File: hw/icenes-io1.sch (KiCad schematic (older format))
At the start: 12 parts

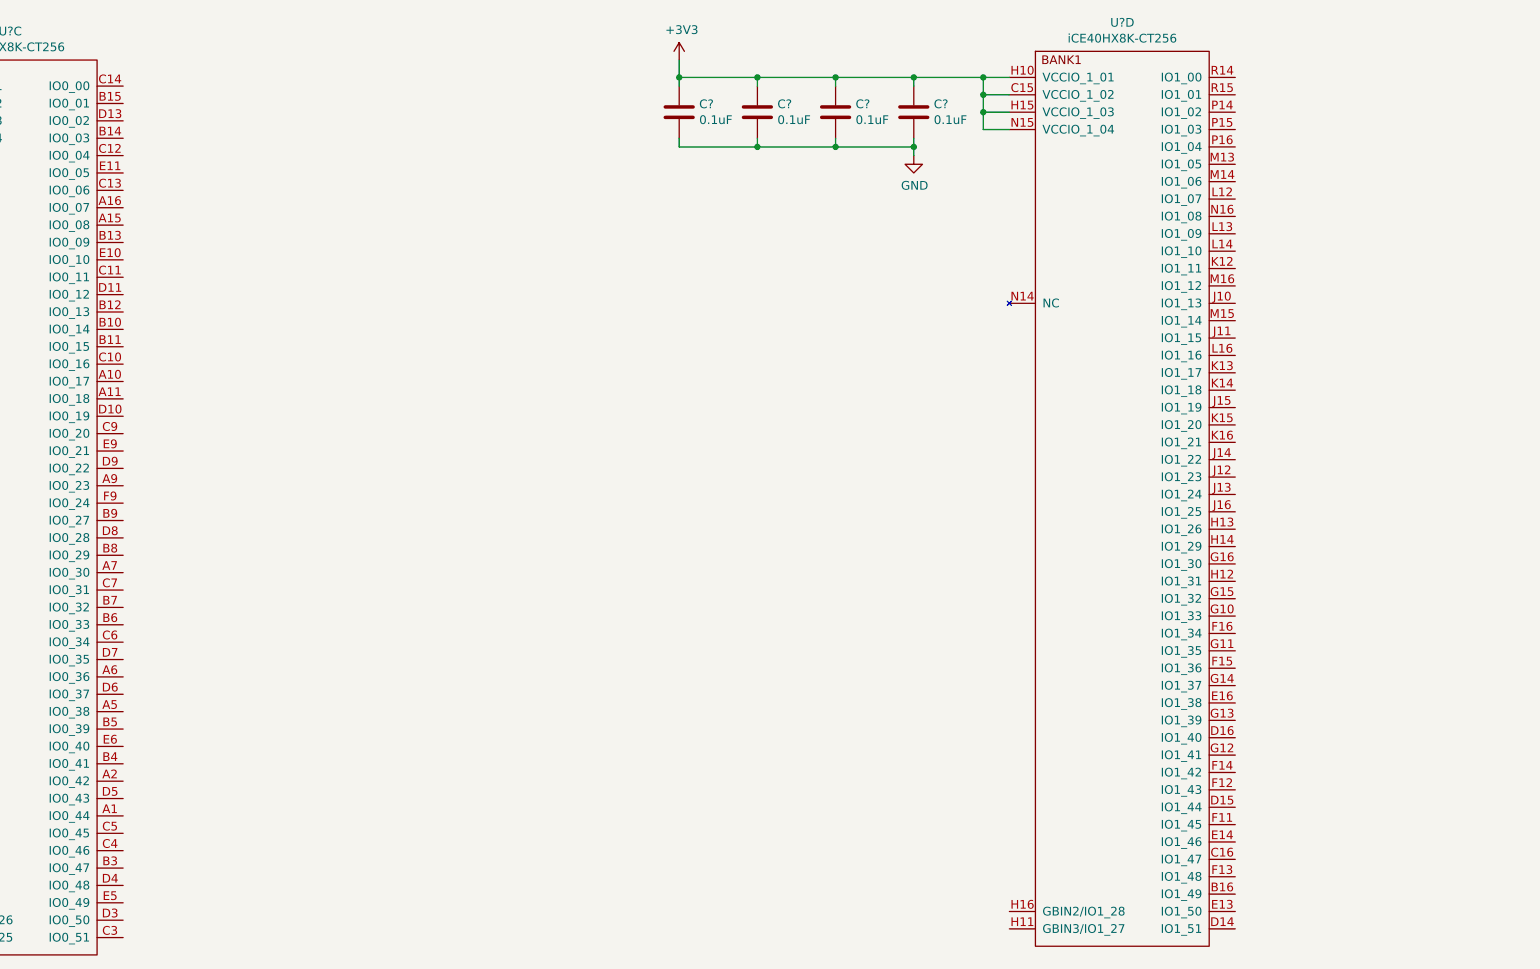
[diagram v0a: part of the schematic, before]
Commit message: Added voltage generators for 3.3V, 1.2V and 5V. Added more info and footprints to some components. Connected signals to the NES connector to banks 0 and 1.
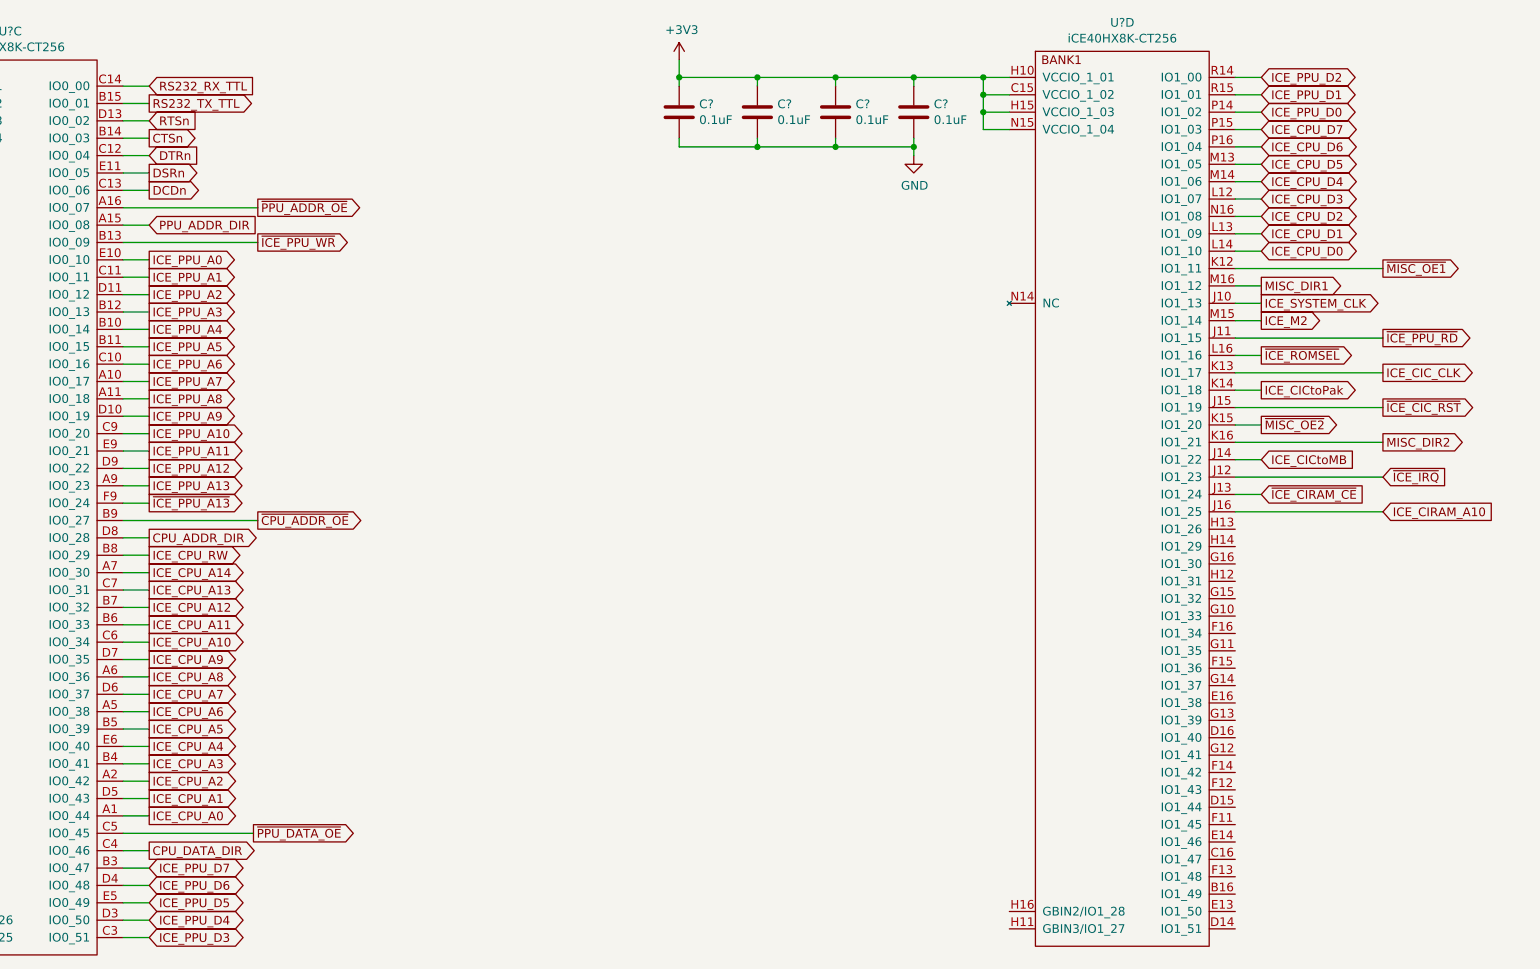
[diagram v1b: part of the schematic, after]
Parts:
- C? (x9): footprint (none) -> Capacitor_SMD:C_0603_1608Metric_Pad1.05x0.95mm_HandSolder; Manufacturer (none) -> Wurth; Part number (none) -> 885012206020
- C?: footprint (none) -> Capacitor_SMD:C_0603_1608Metric_Pad1.05x0.95mm_HandSolder; Manufacturer (none) -> Murata; Part number (none) -> GRM188R61A106KE69D
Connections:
- net ICE_CPU_A0: now reaches U?.A1 (IO0_44)
- net ICE_PPU_A7: now reaches U?.A10 (IO0_17)
- net ICE_PPU_A8: now reaches U?.A11 (IO0_18)
- net PPU_ADDR_DIR: now reaches U?.A15 (IO0_08)
- net ~PPU_ADDR_OE: now reaches U?.A16 (IO0_07)
- net ICE_CPU_A2: now reaches U?.A2 (IO0_42)
- net ICE_CPU_A6: now reaches U?.A5 (IO0_38)
- net ICE_CPU_A8: now reaches U?.A6 (IO0_36)
- net ICE_CPU_A14: now reaches U?.A7 (IO0_30)
- net ICE_PPU_A13: now reaches U?.A9 (IO0_23)
- net ICE_PPU_A4: now reaches U?.B10 (IO0_14)
- net ICE_PPU_A5: now reaches U?.B11 (IO0_15)
- net ICE_PPU_A3: now reaches U?.B12 (IO0_13)
- net ~ICE_PPU_WR: now reaches U?.B13 (IO0_09)
- net CTSn: now reaches U?.B14 (IO0_03)
- net RS232_TX_TTL: now reaches U?.B15 (IO0_01)
- net ICE_PPU_D7: now reaches U?.B3 (IO0_47)
- net ICE_CPU_A3: now reaches U?.B4 (IO0_41)
- net ICE_CPU_A5: now reaches U?.B5 (IO0_39)
- net ICE_CPU_A11: now reaches U?.B6 (IO0_33)
- net ICE_CPU_A12: now reaches U?.B7 (IO0_32)
- net ICE_CPU_RW: now reaches U?.B8 (IO0_29)
- net ~CPU_ADDR_OE: now reaches U?.B9 (IO0_27)
- net ICE_PPU_A6: now reaches U?.C10 (IO0_16)
- net ICE_PPU_A1: now reaches U?.C11 (IO0_11)
- net DTRn: now reaches U?.C12 (IO0_04)
- net DCDn: now reaches U?.C13 (IO0_06)
- net RS232_RX_TTL: now reaches U?.C14 (IO0_00)
- net ICE_PPU_D3: now reaches U?.C3 (IO0_51)
- net CPU_DATA_DIR: now reaches U?.C4 (IO0_46)
- net ~PPU_DATA_OE: now reaches U?.C5 (IO0_45)
- net ICE_CPU_A10: now reaches U?.C6 (IO0_34)
- net ICE_CPU_A13: now reaches U?.C7 (IO0_31)
- net ICE_PPU_A10: now reaches U?.C9 (IO0_20)
- net ICE_PPU_A9: now reaches U?.D10 (IO0_19)
- net ICE_PPU_A2: now reaches U?.D11 (IO0_12)
- net RTSn: now reaches U?.D13 (IO0_02)
- net ICE_PPU_D4: now reaches U?.D3 (IO0_50)
- net ICE_PPU_D6: now reaches U?.D4 (IO0_48)
- net ICE_CPU_A1: now reaches U?.D5 (IO0_43)
- net ICE_CPU_A7: now reaches U?.D6 (IO0_37)
- net ICE_CPU_A9: now reaches U?.D7 (IO0_35)
- net CPU_ADDR_DIR: now reaches U?.D8 (IO0_28)
- net ICE_PPU_A12: now reaches U?.D9 (IO0_22)
- net ICE_PPU_A0: now reaches U?.E10 (IO0_10)
- net DSRn: now reaches U?.E11 (IO0_05)
- net ICE_PPU_D5: now reaches U?.E5 (IO0_49)
- net ICE_CPU_A4: now reaches U?.E6 (IO0_40)
- net ICE_PPU_A11: now reaches U?.E9 (IO0_21)
- net ~ICE_PPU_A13: now reaches U?.F9 (IO0_24)
- net ICE_SYSTEM_CLK: now reaches U?.J10 (IO1_13)
- net ~ICE_PPU_RD: now reaches U?.J11 (IO1_15)
- net ~ICE_IRQ: now reaches U?.J12 (IO1_23)
- net ~ICE_CIRAM_CE: now reaches U?.J13 (IO1_24)
- net ICE_CICtoMB: now reaches U?.J14 (IO1_22)
- net ~ICE_CIC_RST: now reaches U?.J15 (IO1_19)
- net ICE_CIRAM_A10: now reaches U?.J16 (IO1_25)
- net ~MISC_OE1: now reaches U?.K12 (IO1_11)
- net ICE_CIC_CLK: now reaches U?.K13 (IO1_17)
- net ICE_CICtoPak: now reaches U?.K14 (IO1_18)
- net ~MISC_OE2: now reaches U?.K15 (IO1_20)
- net MISC_DIR2: now reaches U?.K16 (IO1_21)
- net ICE_CPU_D3: now reaches U?.L12 (IO1_07)
- net ICE_CPU_D1: now reaches U?.L13 (IO1_09)
- net ICE_CPU_D0: now reaches U?.L14 (IO1_10)
- net ~ICE_ROMSEL: now reaches U?.L16 (IO1_16)
- net ICE_CPU_D5: now reaches U?.M13 (IO1_05)
- net ICE_CPU_D4: now reaches U?.M14 (IO1_06)
- net ICE_M2: now reaches U?.M15 (IO1_14)
- net MISC_DIR1: now reaches U?.M16 (IO1_12)
- net ICE_CPU_D2: now reaches U?.N16 (IO1_08)
- net ICE_PPU_D0: now reaches U?.P14 (IO1_02)
- net ICE_CPU_D7: now reaches U?.P15 (IO1_03)
- net ICE_CPU_D6: now reaches U?.P16 (IO1_04)
- net ICE_PPU_D2: now reaches U?.R14 (IO1_00)
- net ICE_PPU_D1: now reaches U?.R15 (IO1_01)

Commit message: Added 8 LED. Added GPIO header for the rest of the GPIO pins on bank1. Labeled all GPIO pins.
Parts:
- added C? (x3): C10uF, Capacitor_SMD:C_0603_1608Metric_Pad1.05x0.95mm_HandSolder, symbol icenes-library:C10uF
- added D? (x8): Green_LED, LED_SMD:LED_0805_2012Metric_Pad1.15x1.40mm_HandSolder, symbol icenes-library:Green_LED
- added J?: Conn_02x11_Odd_Even, symbol Connector_Generic:Conn_02x11_Odd_Even
- added R? (x8): R698, Resistor_SMD:R_0603_1608Metric_Pad1.05x0.95mm_HandSolder, symbol icenes-library:R698
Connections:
- net labels added: +5V, GPIO_D16, GPIO_E16, GPIO_F12, GPIO_F14, GPIO_F15, GPIO_F16, GPIO_G10, GPIO_G11, GPIO_G12, GPIO_G13, GPIO_G14, GPIO_G15, GPIO_G16, GPIO_H12, GPIO_H13, GPIO_H14, LED1, LED2, LED3, LED4, LED5, LED6, LED7, LED8
- wire segments 135 -> 222
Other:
- moved on the sheet: C?, U?C, U?D

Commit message: GPIO headers for banks 2 and 3.
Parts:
- removed J?: Conn_02x11_Odd_Even, symbol Connector_Generic:Conn_02x11_Odd_Even
- added J?: Conn_02x11_Odd_Even, Connector_PinSocket_2.54mm:PinSocket_2x11_P2.54mm_Vertical, symbol icenes-library:Conn_02x11_Odd_Even
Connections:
- net labels added: LED0
- net labels removed: LED8
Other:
- moved on the sheet: C?

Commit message: Footprints.
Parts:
- U? (x2): Manufacturer (none) -> Lattice; Part number (none) -> iCE40HX8K-CT256
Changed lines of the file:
@@
 F 2 "Package_BGA:BGA-256_14.0x14.0mm_Layout16x16_P0.8mm_Ball0.45mm_Pad0.32mm_NSMD" H 3550 1700 50  0001 C CNN
 F 3 "" H 3550 1700 50  0001 C CNN
+F 4 "Lattice" H 3550 1700 50  0001 C CNN "Manufacturer"
+F 5 "iCE40HX8K-CT256" H 3550 1700 50  0001 C CNN "Part number"
 	3    3550 1700
 	1    0    0    -1
@@
 F 2 "Package_BGA:BGA-256_14.0x14.0mm_Layout16x16_P0.8mm_Ball0.45mm_Pad0.32mm_NSMD" H 10550 1700 50  0001 C CNN
 F 3 "" H 10550 1700 50  0001 C CNN
+F 4 "Lattice" H 10550 1700 50  0001 C CNN "Manufacturer"
+F 5 "iCE40HX8K-CT256" H 10550 1700 50  0001 C CNN "Part number"
 	4    10550 1700
 	1    0    0    -1

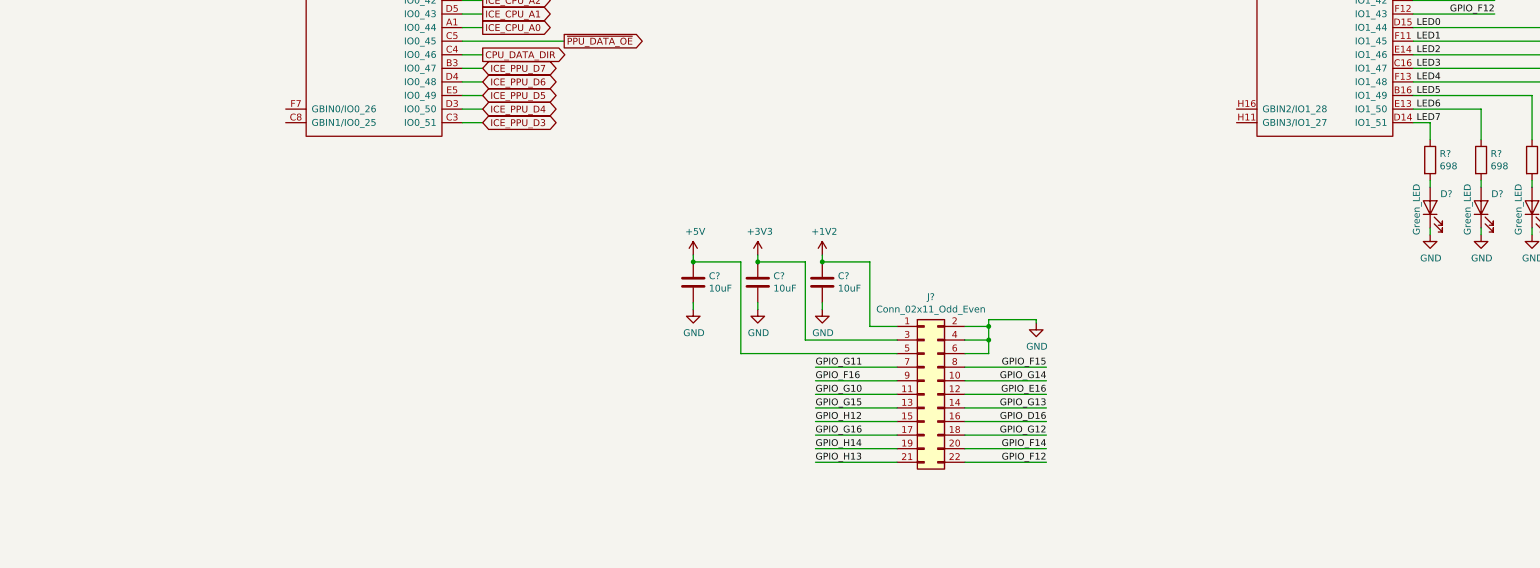
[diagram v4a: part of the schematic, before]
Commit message: Completed USB interface. Clock sources for PAL and NTSC frequencies. Added a 133MHz clock (max input to PLL). Some more stuff.
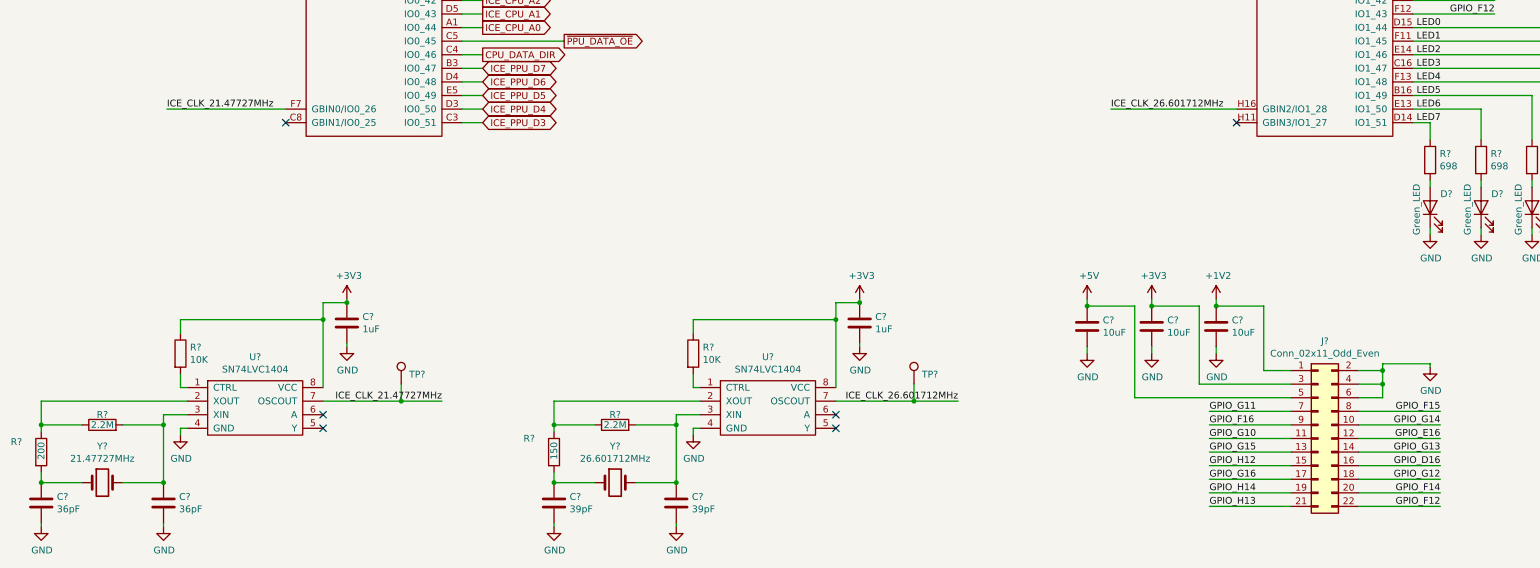
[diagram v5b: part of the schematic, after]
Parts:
- added C? (x2): C1uF, Capacitor_SMD:C_0603_1608Metric_Pad1.05x0.95mm_HandSolder, symbol icenes-library:C1uF
- added C? (x2): C36pF, Capacitor_SMD:C_0603_1608Metric_Pad1.05x0.95mm_HandSolder, symbol icenes-library:C36pF
- added C? (x2): C39pF, Capacitor_SMD:C_0603_1608Metric_Pad1.05x0.95mm_HandSolder, symbol icenes-library:C39pF
- added R? (x2): R10K, Resistor_SMD:R_0603_1608Metric_Pad1.05x0.95mm_HandSolder, symbol icenes-library:R10K
- added R?: R200, Resistor_SMD:R_0603_1608Metric_Pad1.05x0.95mm_HandSolder, symbol icenes-library:R200
- added R? (x2): R2.2M, Resistor_SMD:R_0603_1608Metric_Pad1.05x0.95mm_HandSolder, symbol icenes-library:R2.2M
- added R?: R150, Resistor_SMD:R_0603_1608Metric_Pad1.05x0.95mm_HandSolder, symbol icenes-library:R150
- added TP? (x2): TestPoint, TestPoint:TestPoint_Pad_D1.0mm, symbol icenes-library:TestPoint
- added U? (x2): SN74LVC1404, Package_SO:VSSOP-8_2.3x2mm_P0.5mm, symbol icenes-library:SN74LVC1404
- added Y?: 21.47727MHz, Crystal:Crystal_HC49-4H_Vertical, symbol icenes-library:21.47727MHz
- added Y?: 26.601712MHz, Crystal:Crystal_HC49-4H_Vertical, symbol icenes-library:26.601712MHz
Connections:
- net +3V3: now also C?.1, C?.1, R?.1, R?.1, U?.8 (VCC), U?.8 (VCC)
- net GND: now also C?.2, C?.2, C?.2, C?.2, C?.2, C?.2, U?.4 (GND), U?.4 (GND)
- net ICE_CLK_21.47727MHz: now reaches U?.F7 (GBIN0/IO0_26)
- net ICE_CLK_21.47727MHz: now also TP?.1, U?.7 (OSCOUT)
- net ICE_CLK_26.601712MHz: now reaches U?.H16 (GBIN2/IO1_28)
- net ICE_CLK_26.601712MHz: now also TP?.1, U?.7 (OSCOUT)
- new net: R?.2, U?.1 (CTRL) (x2)
- new net: R?.1, R?.1, U?.2 (XOUT) (x2)
- new net: C?.1, R?.2, U?.3 (XIN), Y?.2 (x2)
- new net: C?.1, R?.2, Y?.1 (x2)
- no-connect marks 0 -> 6
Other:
- moved on the sheet: C?, J?

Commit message: Minor fixes.
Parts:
- gave numbers to parts that had none: 49
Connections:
- net PPU_DATA_DIR: now reaches U4.C8 (GBIN1/IO0_25)
- net ~CPU_DATA_OE: now reaches U4.H11 (GBIN3/IO1_27)
- no-connect marks 6 -> 4
